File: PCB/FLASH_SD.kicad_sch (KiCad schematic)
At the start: 5 parts, among them J1 MEM2090-00-145-00-A_REVA, U4 HSP051-4M10, U5 HSP051-4M10

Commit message: PCB_UPDATE
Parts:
- added U8: MT29F4G08ABBDAH4_D, MT29F4G08ABBDAH4_D:BGA63C80P10X12_900X1100X100N, symbol MT29F4G08ABBDAH4_D:MT29F4G08ABBDAH4_D
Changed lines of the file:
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@@
+	)
+	(symbol
+		(lib_id "MT29F4G08ABBDAH4_D:MT29F4G08ABBDAH4_D")
+		(at 90.17 81.28 0)
+		(unit 1)
+		(exclude_from_sim no)
+		(in_bom yes)
+		(on_board yes)
+		(dnp no)
+		(fields_autoplaced yes)
+		(property "Reference" "U8"
+			(at 90.17 53.34 0)
+			(effects
+				(font
+					(size 1.27 1.27)
+				)
+			)
+		)
+		(property "Value" "MT29F4G08ABBDAH4_D"
+			(at 90.17 55.88 0)
+			(effects
+				(font
+					(size 1.27 1.27)
+				)
+			)
+		)
+		(property "Footprint" "MT29F4G08ABBDAH4_D:BGA63C80P10X12_900X1100X100N"
+			(at 90.17 81.28 0)
+			(effects
+				(font
+					(size 1.27 1.27)
+				)
+				(justify bottom)
+				(hide yes)
+			)
+		)
+		(property "Datasheet" ""
+			(at 90.17 81.28 0)
+			(effects
+				(font
+					(size 1.27 1.27)
+				)
+				(hide yes)
+			)
+		)
+		(property "Description" ""
+			(at 90.17 81.28 0)
+			(effects
+				(font
+					(size 1.27 1.27)
+				)
+				(hide yes)
+			)
+		)
+		(property "MF" "Micron Technology Inc."
+			(at 90.17 81.28 0)
+			(effects
+				(font
+					(size 1.27 1.27)
+				)
+				(justify bottom)
+				(hide yes)
+			)
+		)
+		(property "Description_1" "FLASH - NAND Memory IC 4Gb (512M x 8) Parallel   63-VFBGA (9x11)"
+			(at 90.17 81.28 0)
+			(effects
+				(font
+					(size 1.27 1.27)
+				)
+				(justify bottom)
+				(hide yes)
+			)
+		)
+		(property "Package" "VFBGA-63 Micron Technology"
+			(at 90.17 81.28 0)
+			(effects
+				(font
+					(size 1.27 1.27)
+				)
+				(justify bottom)
+				(hide yes)
+			)
+		)
+		(property "Price" "None"
+			(at 90.17 81.28 0)
+			(effects
+				(font
+					(size 1.27 1.27)
+				)
+				(justify bottom)
+				(hide yes)
+			)
+		)
+		(property "Check_prices" "https://www.snapeda.com/parts/MT29F4G08ABBDAH4:D/Micron/view-part/?ref=eda"
+			(at 90.17 81.28 0)
+			(effects
+				(font
+					(size 1.27 1.27)
+				)
+				(justify bottom)
+				(hide yes)
+			)
+		)
+		(property "SnapEDA_Link" "https://www.snapeda.com/parts/MT29F4G08ABBDAH4:D/Micron/view-part/?ref=snap"
+			(at 90.17 81.28 0)
+			(effects
+				(font
+					(size 1.27 1.27)
+				)
+				(justify bottom)
+				(hide yes)
+			)
+		)
+		(property "MP" "MT29F4G08ABBDAH4:D"
+			(at 90.17 81.28 0)
+			(effects
+				(font
+					(size 1.27 1.27)
+				)
+				(justify bottom)
+				(hide yes)
+			)
+		)
+		(property "Availability" "In Stock"
+			(at 90.17 81.28 0)
+			(effects
+				(font
+					(size 1.27 1.27)
+				)
+				(justify bottom)
+				(hide yes)
+			)
+		)
+		(property "MANUFACTURER" "Micron"
+			(at 90.17 81.28 0)
+			(effects
+				(font
+					(size 1.27 1.27)
+				)
+				(justify bottom)
+				(hide yes)
+			)
+		)
+		(pin "K3"
+		)
+		(pin "K8"
+		)
+		(pin "C4"
+		)
+		(pin "C5"
+		)
+		(pin "F7"
+		)
+		(pin "J6"
+		)
+		(pin "D3"
+		)
+		(pin "K6"
+		)
+		(pin "K5"
+		)
+		(pin "H4"
+		)
+		(pin "C6"
+		)
+		(pin "C3"
+		)
+		(pin "H8"
+		)
+		(pin "K7"
+		)
+		(pin "D4"
+		)
+		(pin "D5"
+		)
+		(pin "J8"
+		)
+		(pin "J4"
+		)
+		(pin "C8"
+		)
+		(pin "J7"
+		)
+		(pin "G4"
+		)
+		(pin "K4"
+		)
+		(pin "C7"
+		)
+		(instances
+			(project ""
+				(path "/65890f61-d586-475b-928a-b635a5e4e59e/ec317a3c-922b-4ac6-af1a-f2cdb70bc7c5"
+					(reference "U8")
+					(unit 1)
+				)
+			)
+		)
 	)
 	(symbol

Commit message: PCB_UPDATE
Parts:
- added C108, C110, C111, C112: 100nF, Capacitor_SMD:C_0402_1005Metric, symbol Device:C
- added C109: 1uF, Capacitor_SMD:C_0402_1005Metric, symbol Device:C
- added R55, R56, R57: 10k, symbol Device:R
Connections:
- net GND: now also U8.C5 (VSS), U8.F7 (VSS), U8.K3 (VSS), U8.K8 (VSS), C108.1, C109.2, C110.1, C111.1, C112.1
- net NAND_NWP: now reaches U8.C3 (WP#)
- net NAND_NWP: now also R56.1
- net NAND_ALE: now reaches U8.C4 (ALE)
- net NAND_NCE: now reaches U8.C6 (CE#)
- net NAND_NCE: now also R55.1
- net NAND_NWE: now reaches U8.C7 (WE#)
- net NAND_NWAIT: now reaches U8.C8 (R/B#)
- net NAND_NWAIT: now also R57.1
- net VDD: now reaches U8.D3 (VCC)
- net VDD: now also U8.G4 (VCC), U8.H8 (VCC), U8.J6 (VCC), C108.2, C109.1, C110.2, C111.2, C112.2, R55.2, R56.2, R57.2
- net NAND_NOE: now reaches U8.D4 (RE#)
- net NAND_CLE: now reaches U8.D5 (CLE)
- net NAND_D0: now reaches U8.H4 (I/O0)
- net NAND_D1: now reaches U8.J4 (I/O1)
- net NAND_D5: now reaches U8.J7 (I/O5)
- net NAND_D7: now reaches U8.J8 (I/O7)
- net NAND_D2: now reaches U8.K4 (I/O2)
- net NAND_D3: now reaches U8.K5 (I/O3)
- net NAND_D4: now reaches U8.K6 (I/O4)
- net NAND_D6: now reaches U8.K7 (I/O6)
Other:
- moved on the sheet: U8

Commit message: PCB_UPDATE
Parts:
- R30, R55, R56, R57: footprint (none) -> Resistor_SMD:R_0402_1005Metric
- U4, U5: footprint HSP051-4M10:IC_HSP051-4M10 -> lib:IC_HSP051-4M10
- U8: footprint MT29F4G08ABBDAH4_D:BGA63C80P10X12_900X1100X100N -> lib:BGA63C80P10X12_900X1100X100N
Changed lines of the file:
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@@
 			)
 		)
-		(property "Footprint" "MT29F4G08ABBDAH4_D:BGA63C80P10X12_900X1100X100N"
+		(property "Footprint" "lib:BGA63C80P10X12_900X1100X100N"
 			(at 86.36 139.7 0)
 			(effects
@@
 			)
 		)
-		(property "Footprint" ""
+		(property "Footprint" "Resistor_SMD:R_0402_1005Metric"
 			(at 181.61 71.628 90)
 			(effects
@@
 			)
 		)
-		(property "Footprint" "HSP051-4M10:IC_HSP051-4M10"
+		(property "Footprint" "lib:IC_HSP051-4M10"
 			(at 255.27 106.68 0)
 			(effects
@@
 			)
 		)
-		(property "Footprint" ""
+		(property "Footprint" "Resistor_SMD:R_0402_1005Metric"
 			(at 38.608 130.81 90)
 			(effects
@@
 			)
 		)
-		(property "Footprint" ""
+		(property "Footprint" "Resistor_SMD:R_0402_1005Metric"
 			(at 29.718 130.81 90)
 			(effects
@@
 			)
 		)
-		(property "Footprint" "HSP051-4M10:IC_HSP051-4M10"
+		(property "Footprint" "lib:IC_HSP051-4M10"
 			(at 210.82 106.68 0)
 			(effects
@@
 			)
 		)
-		(property "Footprint" ""
+		(property "Footprint" "Resistor_SMD:R_0402_1005Metric"
 			(at 55.118 130.81 90)
 			(effects

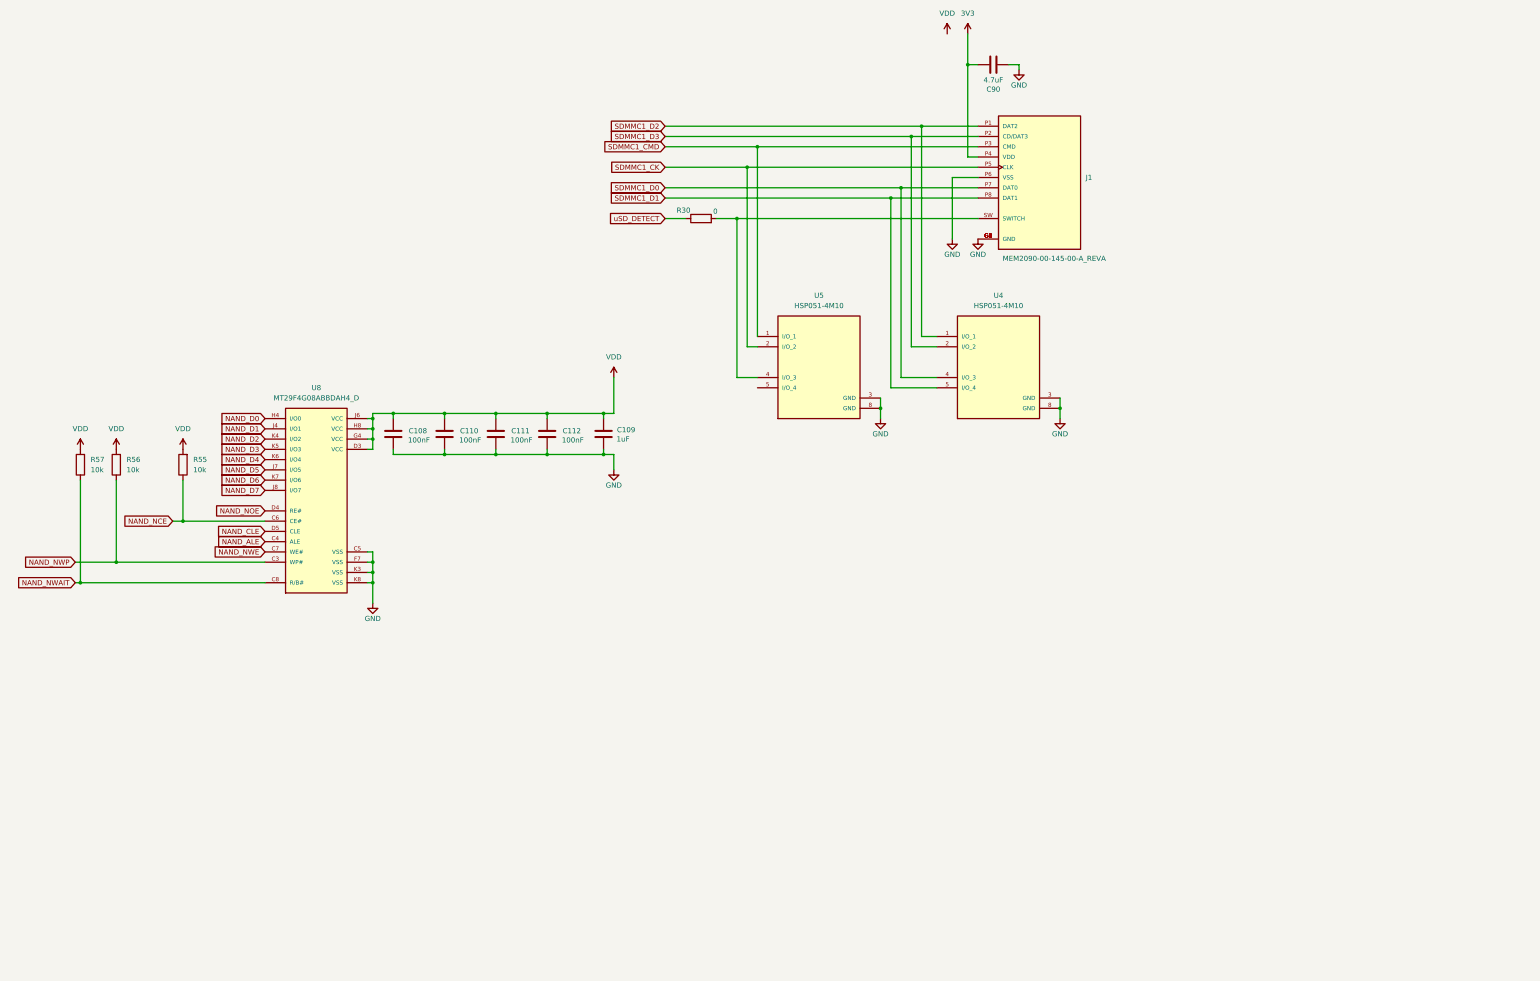
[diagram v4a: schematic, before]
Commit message: added eMMC
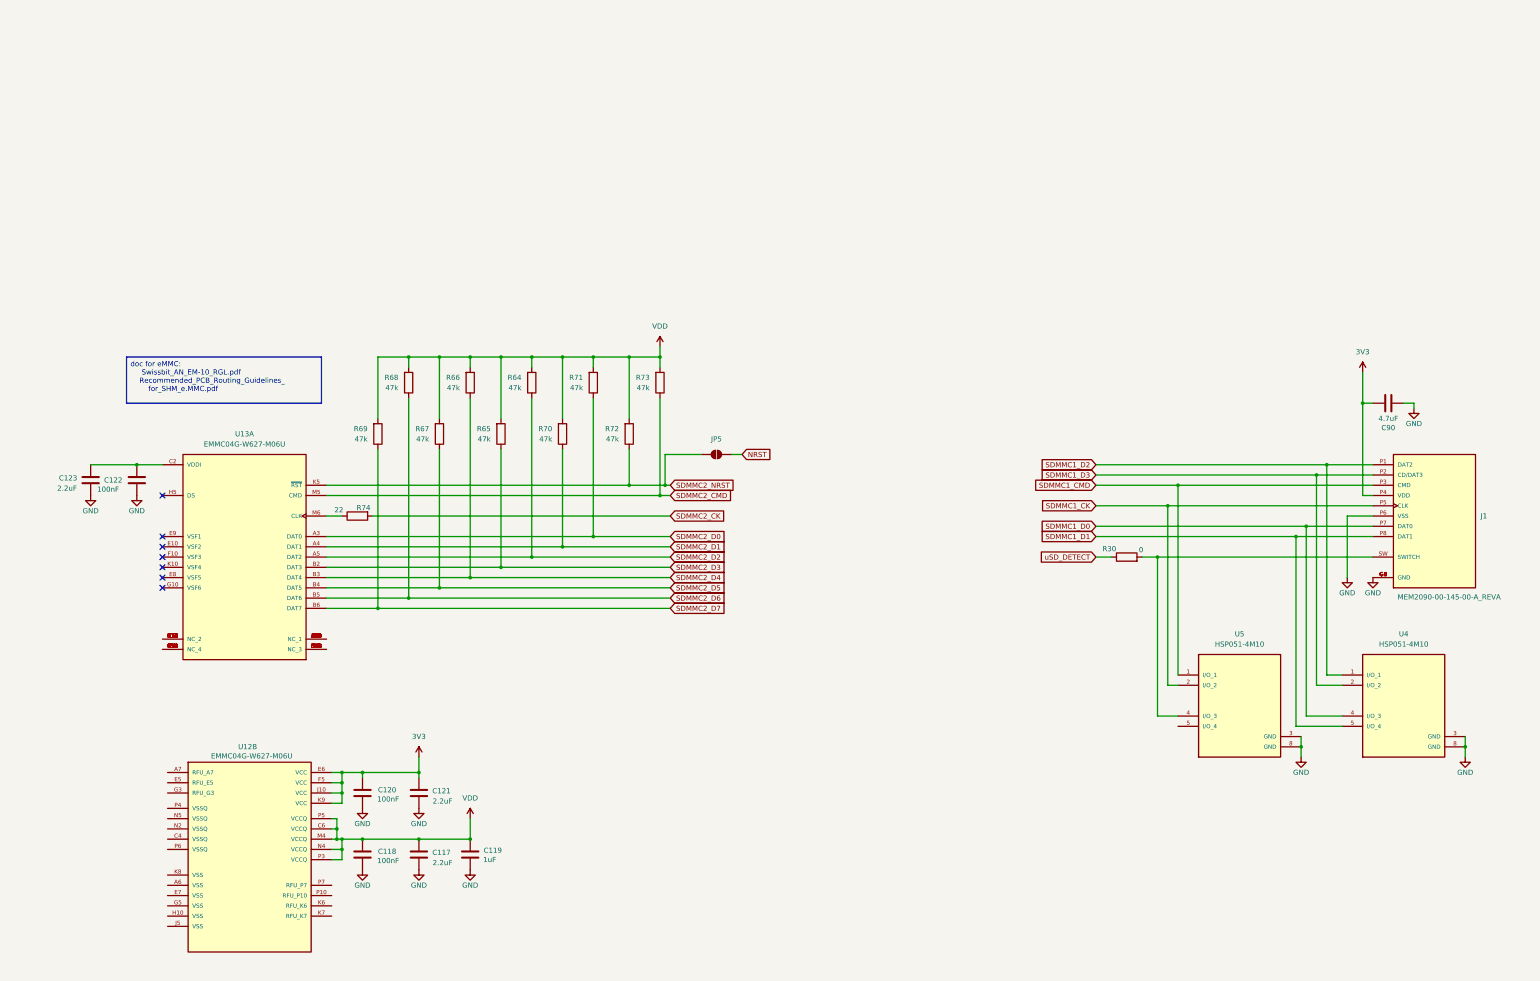
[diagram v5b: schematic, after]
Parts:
- removed C108, C110, C111, C112: 100nF, Capacitor_SMD:C_0402_1005Metric, symbol Device:C
- removed C109: 1uF, Capacitor_SMD:C_0402_1005Metric, symbol Device:C
- removed R55, R56, R57: 10k, Resistor_SMD:R_0402_1005Metric, symbol Device:R
- removed U8: MT29F4G08ABBDAH4_D, lib:BGA63C80P10X12_900X1100X100N, symbol MT29F4G08ABBDAH4_D:MT29F4G08ABBDAH4_D
- added C117, C121, C123: 2.2uF, Capacitor_SMD:C_0402_1005Metric, symbol Device:C
- added C118, C120, C122: 100nF, Capacitor_SMD:C_0402_1005Metric, symbol Device:C
- added C119: 1uF, Capacitor_SMD:C_0402_1005Metric, symbol Device:C
- added JP5: SolderJumper_2_Open, Jumper:SolderJumper-2_P1.3mm_Open_Pad1.0x1.5mm, symbol Jumper:SolderJumper_2_Open
- added R64, R65, R66, R67, R68, R69, R70, R71, R72, R73: 47k, Resistor_SMD:R_0402_1005Metric, symbol Device:R
- added R74: 22, Resistor_SMD:R_0402_1005Metric, symbol Device:R
- added U12, U13: EMMC04G-W627-M06U, EMMC04G-W627-M06U:BGA153N50P14X14_1300X1150X100N, symbol EMMC04G-W627-M06U:EMMC04G-W627-M06U
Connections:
- net 3V3: now also C120.2, C121.1, U12.E6 (VCC), U12.F5 (VCC), U12.J10 (VCC), U12.K9 (VCC)
- net GND: now also C117.2, C118.1, C119.2, C120.1, C121.2, C122.1, C123.2
- net VDD: now also C117.1, C118.2, C119.1, R64.2, R65.2, R66.2, R67.2, R68.2, R69.2, R70.2, R71.2, R72.2, R73.2, U12.C6 (VCCQ), U12.M4 (VCCQ), U12.N4 (VCCQ), U12.P3 (VCCQ), U12.P5 (VCCQ)
- new net: U12.H1 (NC_5), U12.H12 (NC_5), U12.H13 (NC_5), U12.H14 (NC_5), U12.H2 (NC_5), U12.H3 (NC_5), U12.J1 (NC_5), U12.J12 (NC_5), U12.J13 (NC_5), U12.J14 (NC_5), U12.J2 (NC_5), U12.J3 (NC_5), U12.K1 (NC_5), U12.K12 (NC_6), U12.K13 (NC_6), U12.K14 (NC_6), U12.K2 (NC_5), U12.K3 (NC_5), U12.L1 (NC_6), U12.L12 (NC_6), U12.L13 (NC_6), U12.L14 (NC_6), U12.L2 (NC_6), U12.L3 (NC_6), U12.M1 (NC_6), U12.M10 (NC_7), U12.M11 (NC_7), U12.M12 (NC_7), U12.M13 (NC_7), U12.M14 (NC_7), U12.M2 (NC_6), U12.M3 (NC_6), U12.M7 (NC_6), U12.M8 (NC_7), U12.M9 (NC_7), U12.N1 (NC_7), U12.N10 (NC_7), U12.N11 (NC_8), U12.N12 (NC_8), U12.N13 (NC_8), U12.N14 (NC_8), U12.N3 (NC_7), U12.N6 (NC_7), U12.N7 (NC_7), U12.N8 (NC_7), U12.N9 (NC_7), U12.P1 (NC_8), U12.P11 (NC_8), U12.P12 (NC_8), U12.P13 (NC_8), U12.P14 (NC_8), U12.P2 (NC_8), U12.P8 (NC_8), U12.P9 (NC_8)
- new net: C122.2, C123.1, U13.C2 (VDDI)
- new net: U13.A1 (NC_1), U13.A10 (NC_1), U13.A11 (NC_1), U13.A12 (NC_1), U13.A13 (NC_1), U13.A14 (NC_1), U13.A2 (NC_1), U13.A8 (NC_1), U13.A9 (NC_1), U13.B1 (NC_1), U13.B10 (NC_1), U13.B7 (NC_1), U13.B8 (NC_1), U13.B9 (NC_1)
- new net: U13.B11 (NC_2), U13.B12 (NC_2), U13.B13 (NC_2), U13.B14 (NC_2), U13.C1 (NC_2), U13.C10 (NC_2), U13.C11 (NC_2), U13.C12 (NC_2), U13.C13 (NC_2), U13.C14 (NC_2), U13.C3 (NC_2), U13.C5 (NC_2), U13.C7 (NC_2), U13.C8 (NC_2), U13.C9 (NC_2)
- new net: U13.D1 (NC_3), U13.D12 (NC_3), U13.D13 (NC_3), U13.D14 (NC_3), U13.D2 (NC_3), U13.D3 (NC_3), U13.D4 (NC_3), U13.E1 (NC_3), U13.E12 (NC_3), U13.E13 (NC_3), U13.E2 (NC_3), U13.E3 (NC_3)
- new net: U13.E14 (NC_4), U13.F1 (NC_4), U13.F12 (NC_4), U13.F13 (NC_4), U13.F14 (NC_4), U13.F2 (NC_4), U13.F3 (NC_4), U13.G1 (NC_4), U13.G12 (NC_4), U13.G13 (NC_4), U13.G14 (NC_4), U13.G2 (NC_4)
- new net: R74.1, U13.M6 (CLK)
- new net NRST: JP5.2 (B)
- new net SDMMC2_CK: R74.2
- new net SDMMC2_CMD: R73.1, U13.M5 (CMD)
- new net SDMMC2_D0: R71.1, U13.A3 (DAT0)
- new net SDMMC2_D1: R70.1, U13.A4 (DAT1)
- new net SDMMC2_D2: R64.1, U13.A5 (DAT2)
- new net SDMMC2_D3: R65.1, U13.B2 (DAT3)
- new net SDMMC2_D4: R66.1, U13.B3 (DAT4)
- new net SDMMC2_D5: R67.1, U13.B4 (DAT5)
- new net SDMMC2_D6: R68.1, U13.B5 (DAT6)
- new net SDMMC2_D7: R69.1, U13.B6 (DAT7)
- new net SDMMC2_NRST: JP5.1 (A), R72.1, U13.K5 (~{RST})
- no-connect marks 0 -> 7
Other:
- moved on the sheet: C90, J1, R30, U4, U5

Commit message: PCB_UPDATE
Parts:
- U13: footprint EMMC04G-W627-M06U:BGA153N50P14X14_1300X1150X100N -> lib:BGA153N50P14X14_1300X1150X100N
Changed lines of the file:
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@@
 			"FoR8UBFHIOkraiBt3dGSAr2cQLL4RZNsMGJByEfVWL5xFQ75AGgHADCmEXC/T4R8MGJByAe9HCEf"
 			"9HKEfNDLEfJBL0fIB70cIR/0coR80MsR8kEvR8gHvRwhH/RyhHzQyxHyQS9HyAe9HCGf/wfs2dQS"
-			"wV3UugAAAABJRU5ErkJggg=="
+			"wV3UugAAAABJRU5ErkJgggAAAAAAAAAAAAAAAA8AAAAAAAAAAAAAAAAAAAAAAAAAAAAAAAAAAAAA"
+			"AAAAAAAMN1YCAAAAAAAAAAAAAAAAAAAAAAAADwAAAAAAAAAAdGFsaWMAAAAAAAAAAAAAAAAAAAAA"
+			"AAAPAAAAAAAAAABvbnNvbGFzAAAAAAAAAAAAAAAAAAAAAA8AAAAAAAAAAAAAAAAAAAAAAAAAAAAA"
+			"AAAAAAAAAAAAAMR1N1YCAAAAAAAAAAAAAAAAAAAAAAAADwAAAAAAAAAAb2xkAAAAAAAAAAAAAAAA"
+			"AAAAAAAAAAAPAAAAAAAAAABvbnNvbGFzAAAAAAAAAAAAAAAAAAAAAA8AAAAAAAAAAAAAAAAAAAAA"
+			"AAAAAAAAAAAAAAAAAAAAAM91N1YCAAAAAAAAAAAAAAAAAAAAAAAADwAAAAAAAAAAb2xkIEl0YWxp"
+			"YwAAAAAAAAAAAAAAAAAPAAAAAAAAAABvbnNvbGFzAAAAAAAAAAAAAAAAAAAAAA8AAAAAAAAAAAAA"
+			"AAAAAAAAAAAAAAAAAAAAAAAAAAAAAOl1N1YCAAAAAAAAAAAAAAAAAAAAAAAADwAAAAAAAAAAZWd1"
+			"bGFyAAAAAAAAAAAAAAAAAAAAAAAPAAAAAAAAAABvbnNvbGFzAAAAAAAAAAAAAAAAAAAAAA8AAAAA"
+			"AAAAAAAAAAAAAAAAAAAAAAAAAAAAAAAAAAAAAPx1N1YCAAAAAAAAAAAAAAAAAAAAAAAADwAAAAAA"
+			"AAAAdGFsaWMAAAAAAAAAAAAAAAAAAAAAAAAPAAAAAAAAAABvbnNvbGFzAAAAAAAAAAAAAAAAAAAA"
+			"AA8AAAAAAAAAAAAAAAAAAAAAAAAAAAAAAAAAAAAAAAAAAPHeN1YCAAAAAAAAAAAAAAAAAAAAAAAA"
+			"DwAAAAAAAAAAb2xkAAAAAAAAAAAAAAAAAAAAAAAAAAAPAAAAAAAAAABvbnNvbGFzAAAAAAAAAAAA"
+			"AAAAAAAAAA8AAAAAAAAAAAAAAAAAAAAAAAAAAAAAAAAAAAAAAAAAAAXfN1YCAAAAAAAAAAAAAAAA"
+			"AAAAAAAADwAAAAAAAAAAb2xkIEl0YWxpYwAAAAAAAAAAAAAAAAAPAAAAAAAAAABvbnNvbGFzAAAA"
+			"AAAAAAAAAAAAAAAAAA8AAAAAAAAAAAAAAAAAAAAAAAAAAAAAAAAAAAAAAAAAAB7fN1YCAAAAAAAA"
+			"AAAAAAAAAAAAAAAADwAAAAAAAAAAZWd1bGFyAAAAAAAAAAAAAAAAAAAAAAAPAAAAAAAAAABvbnNv"
+			"bGFzAAAAAAAAAAAAAAAAAAAAAA8AAAAAAAAAAAAAAAAAAAAAAAAAAAAAAAAAAAAAAAAAADTfN1YC"
+			"AAAAAAAAAAAAAAAAAAAAAA=="
 		)
 	)
@@
 			"AAAAAAAAAAAAAAAAAAAAAAAAAAAAAAAAAAAAAAAAAAAAAAAAAAAAAAAAAAAAAAAAAAAAAAAAAAAA"
 			"AAAAqbXkAQB+AoAAAAAAAAAAAAAAAAAAAAAAAAAAAAAAAAAAAAAAAAAAAAAAAAAAAAAAAAAAAAAA"
-			"AAAAAAAAAAAAAAAAAAAAAAAAAAAAAAAAAACkteEBAH8CgAAAAA=="
+			"AAAAAAAAAAAAAAAAAAAAAAAAAAAAAAAAAACkteEBAH8CgAAAAAAAAAAAAAAAAAAAAAAAAAAAAAAA"
+			"AAAAAAAAAAAAAAAAAAAAAAAAAAAAAAAAAAAAAAAAAAAAAAAAAAAAAAAAAAAAAAAAAAAAAAAAAAAA"
+			"AAAAAAAAAAAAAAAAAAAAAAAAAAAAAAAAAAAAAAAAAAAAAAAAAAAAAAAAAAAAAAAAAAAAAAAAAAAA"
+			"AAAAAAAAAAAAAAAAAAAAAAAAAAAAAAAAAAAAAAAAAAAAAAAAAAAAAAAAAAAAAAAAAAAAAAAAAAAA"
+			"AAAAAAAAAAAAAAAAAAAAAAAAAAAAAAAAAAAAAAAAAAAAAAAAAAAAAAAAAAAAAAAAAAAAAAAAAAAA"
+			"AAAAAAAAAAAAAAAAAAAAAAAAAAAAAAAAAAAAAAAAAAAAAAAAAAAAAAAAAAAAAAAAAAAAAAAAAAAA"
+			"AAAAAAAAAAAAAAAAAAAAAAAAAAAAAAAAAAAAAAAAAAAAAAAAAAAAAAAAAAAAAAAAAAAAAAAAAAAA"
+			"AAAAAAAAAAAAAAAAAAAAAAAAAAAAAAAAAAAAAAAAAAAAAAAAAAAAAAAAAAAAAAAAAAAAAAAAAAAA"
+			"AAAAAAAAAAAAAAAAAAAAAAAAAAAAAAAAAAAAAAAAAAAAAAAAAAAAAAAAAAAAAAAAAAAAAAAAAAAA"
+			"AAAAAAAAAAAAAAAAAAAAAAAAAAAAAAAAAAAAAAAAAAAAAAAAAAAAAAAAAAAAAAAAAAAAAAAAAAAA"
+			"AAAAAAAAAAAAAAAAAAAAAAAAAAAAAAAAAAAAAAAAAAAAAAAAAAAAAAAAAAAAAAAAAAAAAAAAAAAA"
+			"AAAAAAAAAAAAAAAAAAAAAAAAAAAAAAAAAAAAAAAAAAAAAAAAAAAAAAAAAAAAAAAAAAAAAAAAAAAA"
+			"AAAAAAAAAAAAAAAAAAAAAAAAAAAAAAAAAAAAAAAAAAAAAAAAAAAAAAAAAAAAAAAAAAAAAAAAAAAA"
+			"AAAAAAAAAAAAAAAAAAAAAAAAAAAAAAAAAAAAAAAAAAAAAAAAAAAAAAAAAAAAAAAAAAAAAAAAAAAA"
+			"AAAAAAAAAAAAAAAAAAAAAAAAAAAAAAAAAAAAAAAAAAAAAAAAAAAAAAAAAAAAAAAAAAAAAAAAAAAA"
+			"AAAAAAAAAAAAAAABAAAA/////+IAAAAAAAAAAAAAAAAAAAAcAAAcfMBSAEBgkiRWAgAAsJY0G1YC"
+			"AAAAAAAAAAAAAAAAAAAAAAAAAAAAAAAAAAAAAAAAAAAAAAAAAAAAAAAAAAAAAAAAAAAAAAAAAAAA"
+			"AAAAAAAAAAAAAAAAAAAAAAAAAAAAAAAAAAAAAAAAAAAAAAAAAAAAAAAAAAAAAAAAAAAAAAAAAAAA"
+			"AAAAAAAAAAAAAAAAAAAAAAAAAAAAAAAAAAAAAAAAAAAAAAAAAA=="
 		)
 	)
@@
 			)
 		)
-		(property "Footprint" "EMMC04G-W627-M06U:BGA153N50P14X14_1300X1150X100N"
+		(property "Footprint" "lib:BGA153N50P14X14_1300X1150X100N"
 			(at 68.58 153.67 0)
 			(effects

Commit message: PCB_UPDATE
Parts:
- removed JP5: SolderJumper_2_Open, Jumper:SolderJumper-2_P1.3mm_Open_Pad1.0x1.5mm, symbol Jumper:SolderJumper_2_Open
- removed U12: EMMC04G-W627-M06U, EMMC04G-W627-M06U:BGA153N50P14X14_1300X1150X100N, symbol EMMC04G-W627-M06U:EMMC04G-W627-M06U
- removed U13: EMMC04G-W627-M06U, lib:BGA153N50P14X14_1300X1150X100N, symbol EMMC04G-W627-M06U:EMMC04G-W627-M06U
- added R512: 0, Resistor_SMD:R_0402_1005Metric, symbol Device:R
- added U501: EMMC04G-W627-M06U, lib:BGA153N50P14X14_1300X1150X100N, symbol EMMC04G-W627-M06U:EMMC04G-W627-M06U
- J501: renamed from J1; footprint MEM2090-00-145-00-A_REVA:GCT_MEM2090-00-145-00-A_REVA -> lib:GCT_MEM2090-00-145-00-A_REVA
- renumbered C123 to C501, C122 to C502, C120 to C503, C118 to C504, C121 to C505, C117 to C506, C119 to C507, C90 to C508, R74 to R501, R69 to R502, R68 to R503, R67 to R504, R66 to R505, R65 to R506, R64 to R507, R70 to R508, R71 to R509, R72 to R510, R73 to R511, R30 to R513, U5 to U502, U4 to U503
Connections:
- net 3V3: now also U501.E6 (VCC), U501.F5 (VCC), U501.J10 (VCC), U501.K9 (VCC)
- net GND: now also U501.A6 (VSS), U501.C4 (VSSQ), U501.E7 (VSS), U501.G5 (VSS), U501.H10 (VSS), U501.J5 (VSS), U501.K8 (VSS), U501.N2 (VSSQ), U501.N5 (VSSQ), U501.P4 (VSSQ), U501.P6 (VSSQ)
- net NRST: now also R512.1
- net SDMMC2_CMD: now also U501.M5 (CMD)
- net SDMMC2_D0: now also U501.A3 (DAT0)
- net SDMMC2_D1: now also U501.A4 (DAT1)
- net SDMMC2_D2: now also U501.A5 (DAT2)
- net SDMMC2_D3: now also U501.B2 (DAT3)
- net SDMMC2_D4: now also U501.B3 (DAT4)
- net SDMMC2_D5: now also U501.B4 (DAT5)
- net SDMMC2_D6: now also U501.B5 (DAT6)
- net SDMMC2_D7: now also U501.B6 (DAT7)
- net SDMMC2_NRST: now also R512.2, U501.K5 (~{RST})
- net VDD: now also U501.C6 (VCCQ), U501.M4 (VCCQ), U501.N4 (VCCQ), U501.P3 (VCCQ), U501.P5 (VCCQ)
- net at C501.1, C502.2: now also U501.C2 (VDDI)
- net at R501.1: now also U501.M6 (CLK)
- new net: U501.A1 (NC_1), U501.A10 (NC_1), U501.A11 (NC_1), U501.A12 (NC_1), U501.A13 (NC_1), U501.A14 (NC_1), U501.A2 (NC_1), U501.A8 (NC_1), U501.A9 (NC_1), U501.B1 (NC_1), U501.B10 (NC_1), U501.B7 (NC_1), U501.B8 (NC_1), U501.B9 (NC_1)
- new net: U501.B11 (NC_2), U501.B12 (NC_2), U501.B13 (NC_2), U501.B14 (NC_2), U501.C1 (NC_2), U501.C10 (NC_2), U501.C11 (NC_2), U501.C12 (NC_2), U501.C13 (NC_2), U501.C14 (NC_2), U501.C3 (NC_2), U501.C5 (NC_2), U501.C7 (NC_2), U501.C8 (NC_2), U501.C9 (NC_2)
- new net: U501.D1 (NC_3), U501.D12 (NC_3), U501.D13 (NC_3), U501.D14 (NC_3), U501.D2 (NC_3), U501.D3 (NC_3), U501.D4 (NC_3), U501.E1 (NC_3), U501.E12 (NC_3), U501.E13 (NC_3), U501.E2 (NC_3), U501.E3 (NC_3)
- new net: U501.E14 (NC_4), U501.F1 (NC_4), U501.F12 (NC_4), U501.F13 (NC_4), U501.F14 (NC_4), U501.F2 (NC_4), U501.F3 (NC_4), U501.G1 (NC_4), U501.G12 (NC_4), U501.G13 (NC_4), U501.G14 (NC_4), U501.G2 (NC_4)
- new net: U501.H1 (NC_5), U501.H12 (NC_5), U501.H13 (NC_5), U501.H14 (NC_5), U501.H2 (NC_5), U501.H3 (NC_5), U501.J1 (NC_5), U501.J12 (NC_5), U501.J13 (NC_5), U501.J14 (NC_5), U501.J2 (NC_5), U501.J3 (NC_5), U501.K1 (NC_5), U501.K12 (NC_6), U501.K13 (NC_6), U501.K14 (NC_6), U501.K2 (NC_5), U501.K3 (NC_5), U501.L1 (NC_6), U501.L12 (NC_6), U501.L13 (NC_6), U501.L14 (NC_6), U501.L2 (NC_6), U501.L3 (NC_6), U501.M1 (NC_6), U501.M10 (NC_7), U501.M11 (NC_7), U501.M12 (NC_7), U501.M13 (NC_7), U501.M14 (NC_7), U501.M2 (NC_6), U501.M3 (NC_6), U501.M7 (NC_6), U501.M8 (NC_7), U501.M9 (NC_7), U501.N1 (NC_7), U501.N10 (NC_7), U501.N11 (NC_8), U501.N12 (NC_8), U501.N13 (NC_8), U501.N14 (NC_8), U501.N3 (NC_7), U501.N6 (NC_7), U501.N7 (NC_7), U501.N8 (NC_7), U501.N9 (NC_7), U501.P1 (NC_8), U501.P11 (NC_8), U501.P12 (NC_8), U501.P13 (NC_8), U501.P14 (NC_8), U501.P2 (NC_8), U501.P8 (NC_8), U501.P9 (NC_8)
- no-connect marks 7 -> 14
